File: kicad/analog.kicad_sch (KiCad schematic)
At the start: 74 parts, among them J701 AI 1-10, J702 mA SELECT, J703 AI PWR/COM

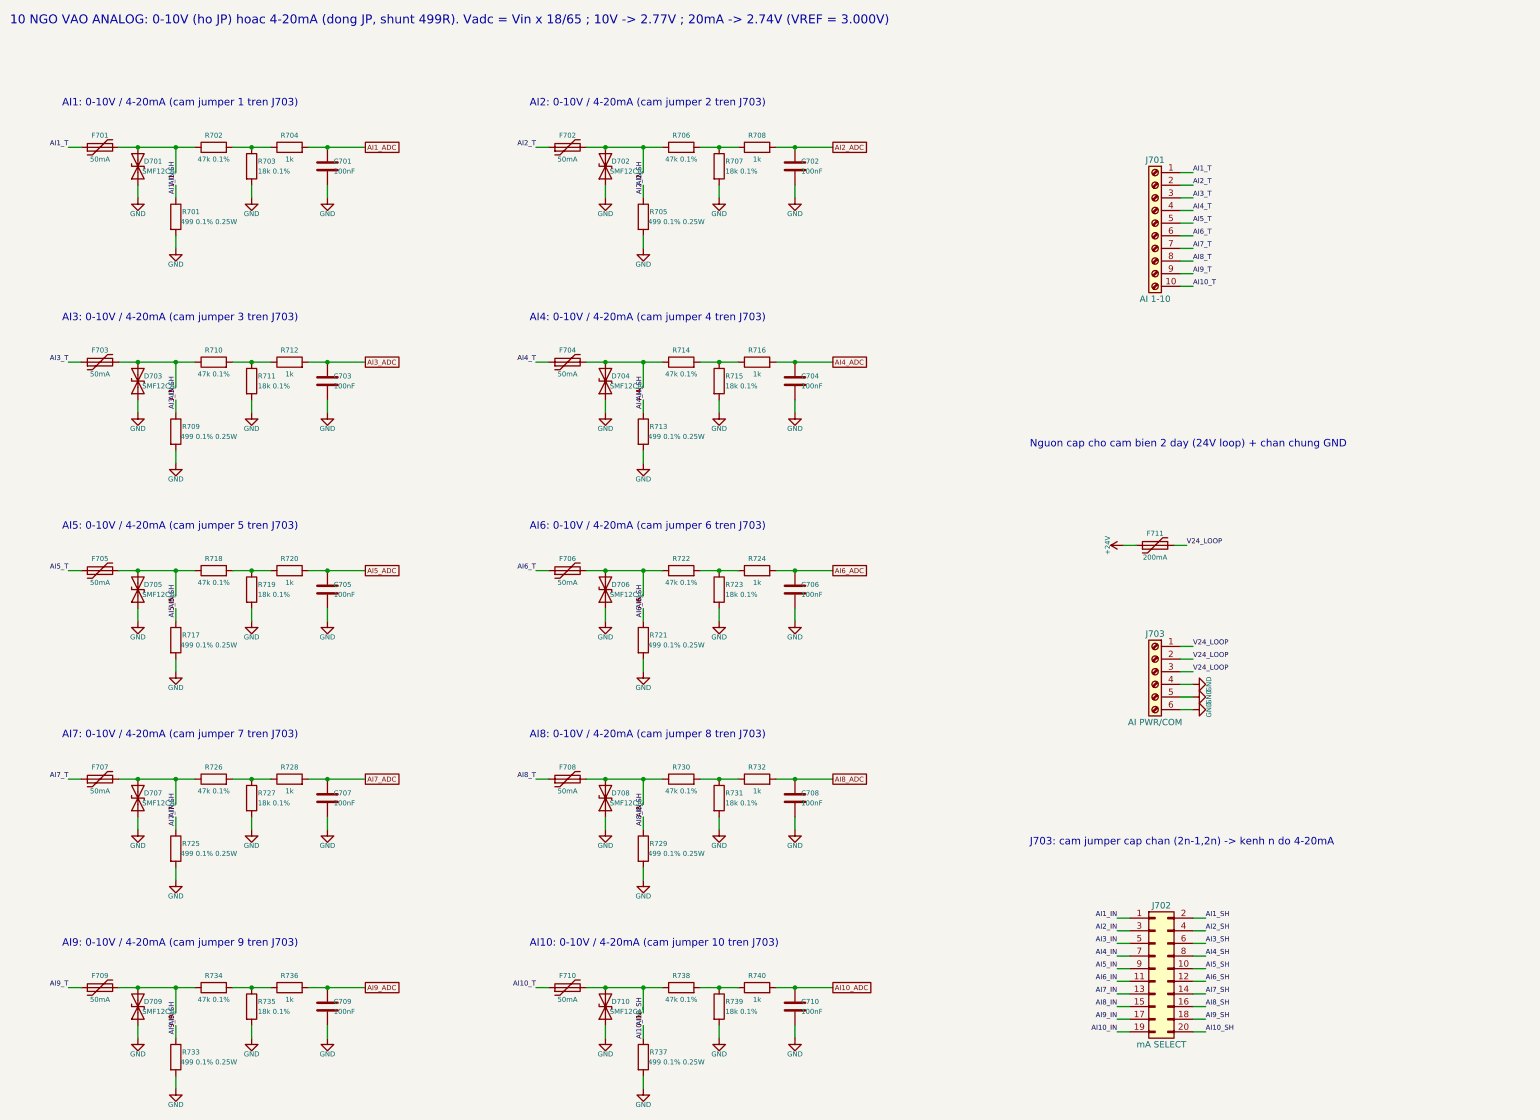
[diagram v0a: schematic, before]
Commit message: - bỏ các mạch 0-10v, RS485 RTU
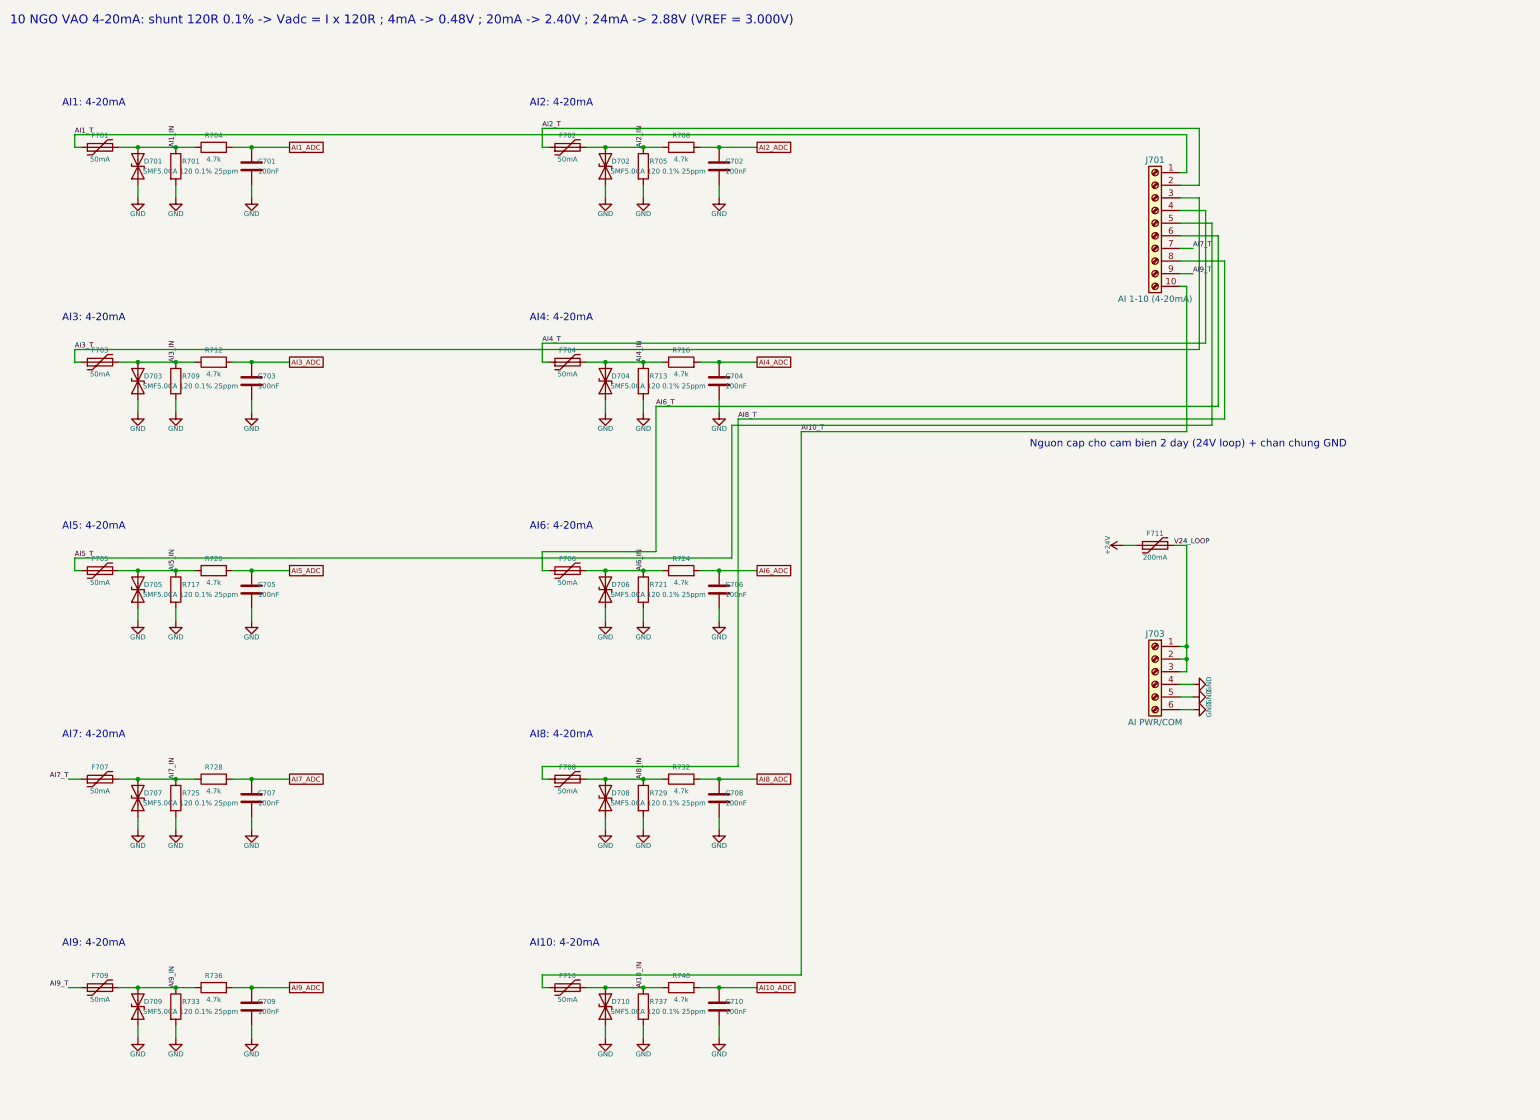
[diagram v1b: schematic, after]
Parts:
- removed J702: mA SELECT, Connector_PinHeader_2.54mm:PinHeader_2x10_P2.54mm_Vertical, symbol Connector_Generic:Conn_02x10_Odd_Even
- removed R702, R706, R710, R714, R718, R722, R726, R730, R734, R738: 47k 0.1%, Resistor_SMD:R_0603_1608Metric, symbol Device:R
- removed R703, R707, R711, R715, R719, R723, R727, R731, R735, R739: 18k 0.1%, Resistor_SMD:R_0603_1608Metric, symbol Device:R
- D701, D702, D703, D704, D705, D706, D707, D708, D709, D710: value SMF12CA -> SMF5.0CA
- J701: value AI 1-10 -> AI 1-10 (4-20mA)
- R701, R705, R709, R713, R717, R721, R725, R729, R733, R737: value 499 0.1% 0.25W -> 120 0.1% 25ppm
- R704, R708, R712, R716, R720, R724, R728, R732, R736, R740: value 1k -> 4.7k
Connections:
- net AI10_SH is gone; now on net AI10_IN: R737.1
- net AI1_SH is gone; now on net AI1_IN: R701.1
- net AI2_SH is gone; now on net AI2_IN: R705.1
- net AI3_SH is gone; now on net AI3_IN: R709.1
- net AI4_SH is gone; now on net AI4_IN: R713.1
- net AI5_SH is gone; now on net AI5_IN: R717.1
- net AI6_SH is gone; now on net AI6_IN: R721.1
- net AI7_SH is gone; now on net AI7_IN: R725.1
- net AI8_SH is gone; now on net AI8_IN: R729.1
- net AI9_SH is gone; now on net AI9_IN: R733.1
- net AI10_IN: now also R740.1
- net AI1_IN: now also R704.1
- net AI2_IN: now also R708.1
- net AI3_IN: now also R712.1
- net AI4_IN: now also R716.1
- net AI5_IN: now also R720.1
- net AI6_IN: now also R724.1
- net AI7_IN: now also R728.1
- net AI8_IN: now also R732.1
- net AI9_IN: now also R736.1
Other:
- note added: "10 NGO VAO 4-20mA: shunt 120R 0.1% -> Vadc = I x 120R ; 4mA -> 0.48V ; 20mA -> 2.40V ; 24mA -> 2.88V (VREF = 3.000V)"
- note added: "AI10: 4-20mA"
- note added: "AI1: 4-20mA"
- note added: "AI2: 4-20mA"
- note added: "AI3: 4-20mA"
- note added: "AI4: 4-20mA"
- note added: "AI5: 4-20mA"
- note added: "AI6: 4-20mA"
- note added: "AI7: 4-20mA"
- note added: "AI8: 4-20mA"
- note added: "AI9: 4-20mA"
- note removed: "10 NGO VAO ANALOG: 0-10V (ho JP) hoac 4-20mA (dong JP, shunt 499R). Vadc = Vin x 18/65 ; 10V -> 2.77V ; 20mA -> 2.74V (VREF = 3.000V)"
- note removed: "AI10: 0-10V / 4-20mA (cam jumper 10 tren J703)"
- note removed: "AI1: 0-10V / 4-20mA (cam jumper 1 tren J703)"
- note removed: "AI2: 0-10V / 4-20mA (cam jumper 2 tren J703)"
- note removed: "AI3: 0-10V / 4-20mA (cam jumper 3 tren J703)"
- note removed: "AI4: 0-10V / 4-20mA (cam jumper 4 tren J703)"
- note removed: "AI5: 0-10V / 4-20mA (cam jumper 5 tren J703)"
- note removed: "AI6: 0-10V / 4-20mA (cam jumper 6 tren J703)"
- note removed: "AI7: 0-10V / 4-20mA (cam jumper 7 tren J703)"
- note removed: "AI8: 0-10V / 4-20mA (cam jumper 8 tren J703)"
- note removed: "AI9: 0-10V / 4-20mA (cam jumper 9 tren J703)"
- note removed: "J703: cam jumper cap chan (2n-1,2n) -> kenh n do 4-20mA"
- title: 10 ngo vao analog 0-10V / 4-20mA -> 10 ngo vao analog 4-20mA

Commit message: - bỏ các cầu chì thêm mô tả cho từng linh kiên
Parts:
- removed F701, F702, F703, F704, F705, F706, F707, F708, F709, F710: 50mA, Fuse:Fuse_0805_2012Metric, symbol Device:Polyfuse
- F711: value 200mA -> MF-MSMF050-2 0.5A/60V; footprint Fuse:Fuse_1206_3216Metric -> Fuse:Fuse_1812_4532Metric
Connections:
- net AI10_T is gone; now on net AI10_IN: J701.10 (Pin_10)
- net AI1_T is gone; now on net AI1_IN: J701.1 (Pin_1)
- net AI2_T is gone; now on net AI2_IN: J701.2 (Pin_2)
- net AI3_T is gone; now on net AI3_IN: J701.3 (Pin_3)
- net AI4_T is gone; now on net AI4_IN: J701.4 (Pin_4)
- net AI5_T is gone; now on net AI5_IN: J701.5 (Pin_5)
- net AI6_T is gone; now on net AI6_IN: J701.6 (Pin_6)
- net AI7_T is gone; now on net AI7_IN: J701.7 (Pin_7)
- net AI8_T is gone; now on net AI8_IN: J701.8 (Pin_8)
- net AI9_T is gone; now on net AI9_IN: J701.9 (Pin_9)
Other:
- note added: "Cảm biến 2 dây: V24_LOOP → (+) → (−) → AIn. 4 dây: ngõ ra mA → AIn, 0V cảm biến → GND."
- note added: "F711 PTC 0.5A/60V (MF-MSMF050-2): bảo vệ nguồn 24V nuôi cảm biến; 10 × 24mA = 240mA < 0.5A."
- note added: "Firmware: I(mA) = raw/4095 × 3000mV/120Ω. Dải 4–20mA ≈ 2600 mức ADC."
- note added: "J701: AI1–AI10 nối thẳng vào kênh (đã bỏ cầu chì từng kênh)."
- note added: "KÊNH 4–20mA (10 kênh giống nhau)"
- note added: "RC 4.7k/100nF: f_c = 1/(2πRC) ≈ 340Hz; hạn dòng vào ADC ≈ 1mA khi quá áp."
- note added: "Shunt 120Ω 0.1%: V = I·R; R ≤ 3.0V/24mA = 125Ω → 120Ω. 4mA → 0.48V, 20mA → 2.40V; P = 48mW."
- note added: "TVS SMF5.0CA: kẹp xung/quá áp > 5V. Không có cầu chì: đấu nhầm 24V vào AIn → 200mA, 4.8W → cháy shunt."
